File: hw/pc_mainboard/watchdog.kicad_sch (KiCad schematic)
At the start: 0 parts

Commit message: Watchdog research
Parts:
- added U7: watchdog_STWD100NYWY3F, STWD100NYWY3F:SOP95P280X145-5N, symbol pc_mainboard:watchdog_STWD100NYWY3F
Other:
- title: (none) -> Watchdog
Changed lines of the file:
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@@
 	(generator_version "8.0")
 	(paper "A4")
+	(title_block
+		(title "Watchdog")
+	)
+	(symbol
+		(lib_id "pc_mainboard:watchdog_STWD100NYWY3F")
+		(at 146.05 93.98 0)
+		(unit 1)
+		(exclude_from_sim no)
+		(in_bom yes)
+		(on_board yes)
+		(dnp no)
+		(fields_autoplaced yes)
+		(property "Reference" "U7"
+			(at 146.05 81.28 0)
+			(effects
+				(font
+					(size 1.27 1.27)
+				)
+			)
+		)
+		(property "Value" "watchdog_STWD100NYWY3F"
+			(at 146.05 83.82 0)
+			(effects
+				(font
+					(size 1.27 1.27)
+				)
+			)
+		)
+		(property "Footprint" "STWD100NYWY3F:SOP95P280X145-5N"
+			(at 146.05 93.98 0)
+			(effects
+				(font
+					(size 1.27 1.27)
+				)
+				(justify bottom)
+				(hide yes)
+			)
+		)
+		(property "Datasheet" ""
+			(at 146.05 93.98 0)
+			(effects
+				(font
+					(size 1.27 1.27)
+				)
+				(hide yes)
+			)
+		)
+		(property "Description" ""
+			(at 146.05 93.98 0)
+			(effects
+				(font
+					(size 1.27 1.27)
+				)
+				(hide yes)
+			)
+		)
+		(property "PARTREV" "11"
+			(at 146.05 93.98 0)
+			(effects
+				(font
+					(size 1.27 1.27)
+				)
+				(justify bottom)
+				(hide yes)
+			)
+		)
+		(property "STANDARD" "IPC-7351B"
+			(at 146.05 93.98 0)
+			(effects
+				(font
+					(size 1.27 1.27)
+				)
+				(justify bottom)
+				(hide yes)
+			)
+		)
+		(property "MAXIMUM_PACKAGE_HEIGHT" "1.45mm"
+			(at 146.05 93.98 0)
+			(effects
+				(font
+					(size 1.27 1.27)
+				)
+				(justify bottom)
+				(hide yes)
+			)
+		)
+		(property "MANUFACTURER" "ST Microelectronics"
+			(at 146.05 93.98 0)
+			(effects
+				(font
+					(size 1.27 1.27)
+				)
+				(justify bottom)
+				(hide yes)
+			)
+		)
+		(pin "2"
+		)
+		(pin "1"
+		)
+		(pin "5"
+		)
+		(pin "3"
+		)
+		(pin "4"
+		)
+		(instances
+			(project ""
+				(path "/69a74940-cd00-4a75-bd5b-2bda9e86219a/977b4f9e-3c82-4114-8a79-574bf38f2b4c"
+					(reference "U7")
+					(unit 1)
+				)
+			)
+		)
+	)
 )

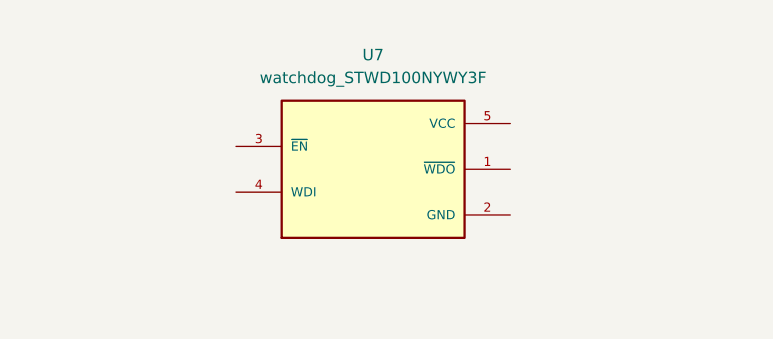
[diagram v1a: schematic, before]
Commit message: Watchdog schematic capture
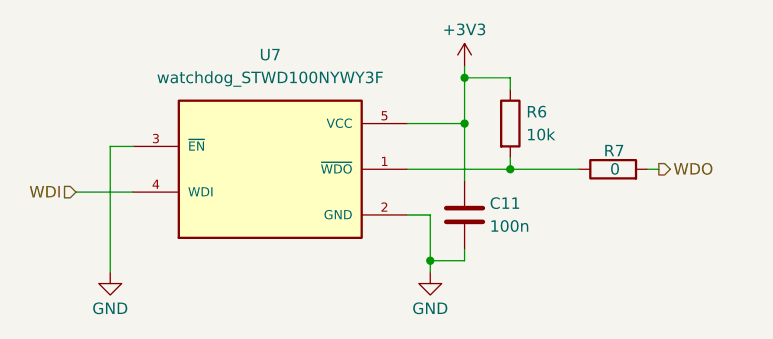
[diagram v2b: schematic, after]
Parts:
- added C11: 100n, symbol Device:C
- added R6: 10k, symbol Device:R
- added R7: 0, symbol Device:R
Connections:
- net at U7.1 (~{WDO}): now also R6.2, R7.1
- net GND: now reaches U7.2 (GND)
- net GND: now also U7.3 (~{EN}), C11.2
- net WDI: now reaches U7.4 (WDI)
- net +3V3: now reaches U7.5 (VCC)
- net +3V3: now also C11.1, R6.1
- new net WDO: R7.2
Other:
- moved on the sheet: U7

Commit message: RAM Schematic Capture (#39)
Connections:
- net WDO renamed ~{WDO}
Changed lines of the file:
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@@
 		)
 	)
-	(hierarchical_label "WDO"
+	(hierarchical_label "~{WDO}"
 		(shape output)
 		(at 177.8 93.98 0)

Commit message: Schematic capture Flash
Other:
- moved on the sheet: R7
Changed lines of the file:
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@@
 	(wire
 		(pts
-			(xy 161.29 93.98) (xy 168.91 93.98)
+			(xy 161.29 93.98) (xy 167.64 93.98)
 		)
 		(stroke
@@
 	(wire
 		(pts
-			(xy 176.53 93.98) (xy 177.8 93.98)
+			(xy 175.26 93.98) (xy 177.8 93.98)
 		)
 		(stroke
@@
 	(symbol
 		(lib_id "Device:R")
-		(at 172.72 93.98 90)
+		(at 171.45 93.98 90)
 		(unit 1)
 		(exclude_from_sim no)
@@
 		(dnp no)
 		(property "Reference" "R7"
-			(at 173.99 91.948 90)
+			(at 172.72 91.948 90)
 			(effects
 				(font
@@
 		)
 		(property "Value" "0"
-			(at 173.482 93.98 90)
+			(at 172.212 93.98 90)
 			(effects
 				(font
@@
 		)
 		(property "Footprint" ""
-			(at 172.72 95.758 90)
+			(at 171.45 95.758 90)
 			(effects
 				(font
@@
 		)
 		(property "Datasheet" "~"
-			(at 172.72 93.98 0)
+			(at 171.45 93.98 0)
 			(effects
 				(font
@@
 		)
 		(property "Description" "Resistor"
-			(at 172.72 93.98 0)
-			(effects
-				(font
+			(at 171.45 93.98 0)
+			(effects
+				(font
